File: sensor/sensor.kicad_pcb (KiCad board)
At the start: 2 copper layers, 46.5 x 34 mm, 42 parts, among them J1 5V, J2 CAN IN, J3 CAN OUT, J4 AVR-ISP-6, J5 SENSOR IN, J6 SENSOR VCC, J7 SENSOR GND, U1 ATmega32M1-AU, U2 MCP2551-I-SN, Y1 16MHz

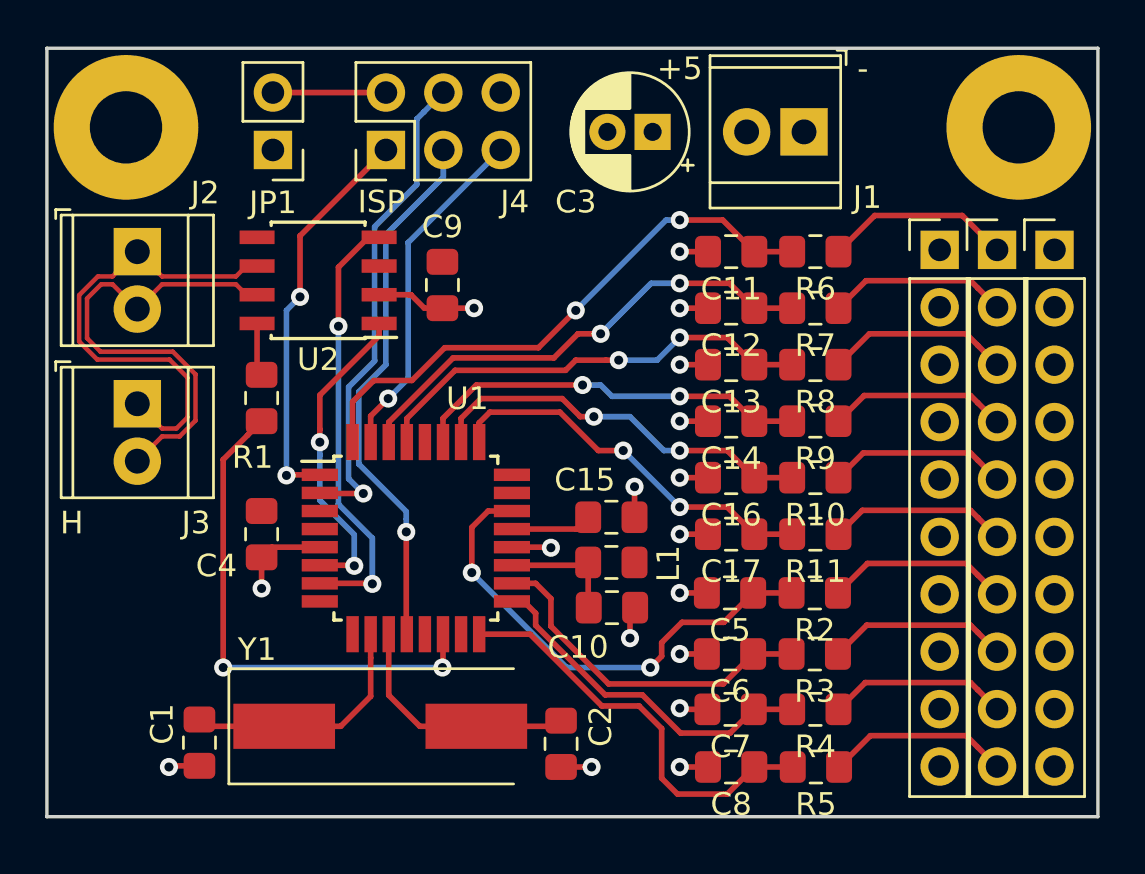
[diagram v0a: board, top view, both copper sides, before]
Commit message: Added power LED to sensor board
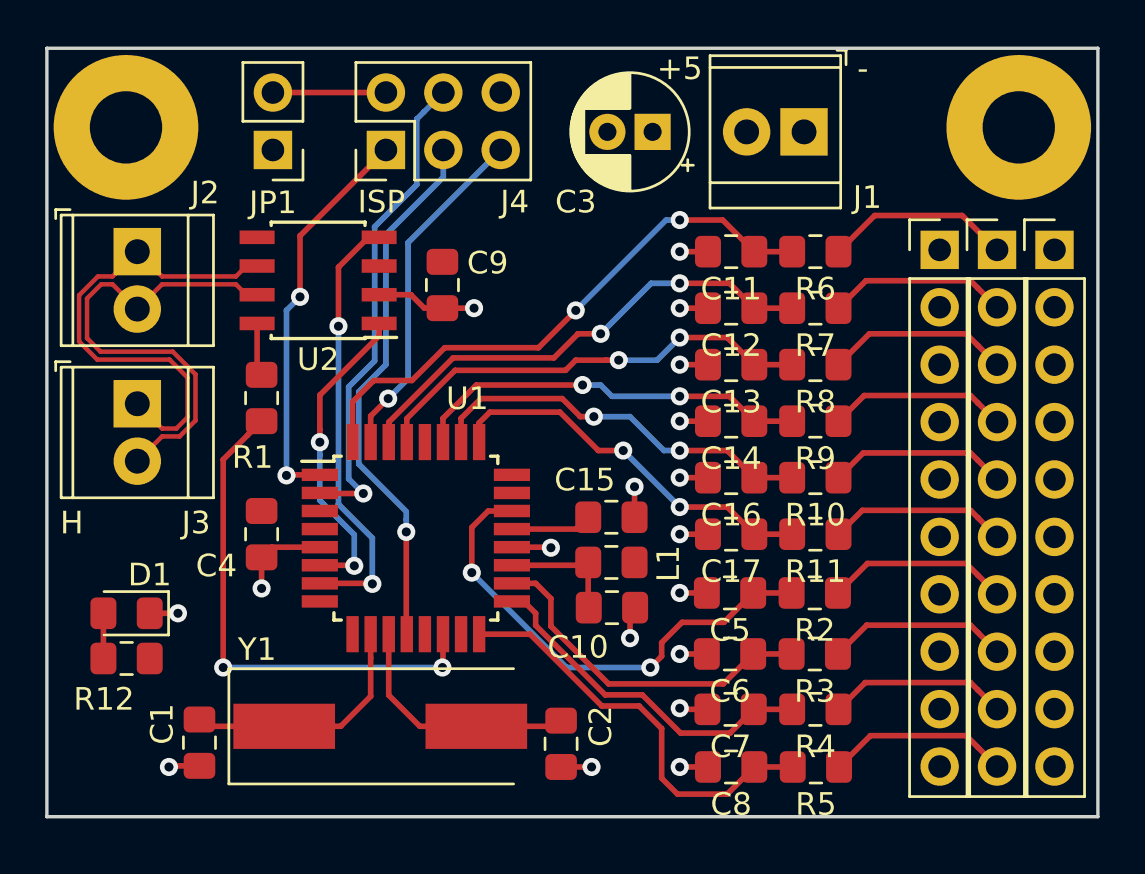
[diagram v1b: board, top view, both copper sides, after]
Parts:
- added D1: POWER, LED_SMD:LED_0805_2012Metric_Pad1.15x1.40mm_HandSolder, F.Cu at (126.5, 87.0)
- added R12: 470, Resistor_SMD:R_0805_2012Metric_Pad1.15x1.40mm_HandSolder, F.Cu at (126.5, 89.0)
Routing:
- net Net-(D1-Pad2): track 0.00 -> 2.00 mm
- net GND: track 28.2 -> 29.5 mm, vias 17 -> 18
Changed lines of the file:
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@@
     (thickness 1.6)
     (drawings 10)
-    (tracks 312)
+    (tracks 315)
     (zones 0)
-    (modules 42)
-    (nets 38)
+    (modules 44)
+    (nets 39)
   )
   (page A4)
@@
   (net 36 /CAN_TXD)
   (net 37 /CAN_RXD)
+  (net 38 "Net-(D1-Pad2)")
   (net_class Default "This is the default net class."
     (clearance 0.2)
@@
     (add_net "Net-(C1-Pad1)")
     (add_net "Net-(C2-Pad2)")
+    (add_net "Net-(D1-Pad2)")
     (add_net "Net-(J4-Pad2)")
     (add_net "Net-(R1-Pad1)")
@@
     (tags "capacitor handsolder")
     (attr smd)
-    (fp_text reference C9 (at -2.575 0) (layer F.SilkS)
+    (fp_text reference C9 (at -0.975 -2) (layer F.SilkS)
       (effects (font (size 1 1) (thickness 0.15)))
     )
@@
     (pad 1 thru_hole circle (at 0 0) (size 6.4 6.4) (drill 3.2) (layers *.Cu *.Mask)
       (net 2 GND))
+  )
+  (module LED_SMD:LED_0805_2012Metric_Pad1.15x1.40mm_HandSolder (layer F.Cu)
+    (at 126.525 87 180)
+    (descr "LED SMD 0805 (2012 Metric), square (rectangular) end terminal, IPC_7351 nominal, (Body size source: https://docs.google.com/spreadsheets/d/1BsfQQcO9C6DZCsRaXUlFlo91Tg2WpOkGARC1WS5S8t0/edit?usp=sharing), generated with kicad-footprint-generator")
+    (tags "LED handsolder")
+    (attr smd)
+    (fp_text reference D1 (at -1.025 1.7 180) (layer F.SilkS)
+      (effects (font (size 1 1) (thickness 0.15)))
+    )
+    (fp_text value POWER (at 0 1.65 180) (layer F.Fab)
+      (effects (font (size 1 1) (thickness 0.15)))
+    )
+    (fp_line (start 1 -0.6) (end -0.7 -0.6) (layer F.Fab) (width 0.1))
+    (fp_line (start -0.7 -0.6) (end -1 -0.3) (layer F.Fab) (width 0.1))
+    (fp_line (start -1 -0.3) (end -1 0.6) (layer F.Fab) (width 0.1))
+    (fp_line (start -1 0.6) (end 1 0.6) (layer F.Fab) (width 0.1))
+    (fp_line (start 1 0.6) (end 1 -0.6) (layer F.Fab) (width 0.1))
+    (fp_line (start 1 -0.96) (end -1.86 -0.96) (layer F.SilkS) (width 0.12))
+    (fp_line (start -1.86 -0.96) (end -1.86 0.96) (layer F.SilkS) (width 0.12))
+    (fp_line (start -1.86 0.96) (end 1 0.96) (layer F.SilkS) (width 0.12))
+    (fp_line (start -1.85 0.95) (end -1.85 -0.95) (layer F.CrtYd) (width 0.05))
+    (fp_line (start -1.85 -0.95) (end 1.85 -0.95) (layer F.CrtYd) (width 0.05))
+    (fp_line (start 1.85 -0.95) (end 1.85 0.95) (layer F.CrtYd) (width 0.05))
+    (fp_line (start 1.85 0.95) (end -1.85 0.95) (layer F.CrtYd) (width 0.05))
+    (fp_text user %R (at 0 0 180) (layer F.Fab)
+      (effects (font (size 0.5 0.5) (thickness 0.08)))
+    )
+    (pad 1 smd roundrect (at -1.025 0 180) (size 1.15 1.4) (layers F.Cu F.Paste F.Mask) (roundrect_rratio 0.217391)
+      (net 2 GND))
+    (pad 2 smd roundrect (at 1.025 0 180) (size 1.15 1.4) (layers F.Cu F.Paste F.Mask) (roundrect_rratio 0.217391)
+      (net 38 "Net-(D1-Pad2)"))
+    (model ${KISYS3DMOD}/LED_SMD.3dshapes/LED_0805_2012Metric.wrl
+      (at (xyz 0 0 0))
+      (scale (xyz 1 1 1))
+      (rotate (xyz 0 0 0))
+    )
+  )
+  (module Resistor_SMD:R_0805_2012Metric_Pad1.15x1.40mm_HandSolder (layer F.Cu)
+    (at 126.525 89)
+    (descr "Resistor SMD 0805 (2012 Metric), square (rectangular) end terminal, IPC_7351 nominal with elongated pad for handsoldering. (Body size source: https://docs.google.com/spreadsheets/d/1BsfQQcO9C6DZCsRaXUlFlo91Tg2WpOkGARC1WS5S8t0/edit?usp=sharing), generated with kicad-footprint-generator")
+    (tags "resistor handsolder")
+    (attr smd)
+    (fp_text reference R12 (at -1 1.8 180) (layer F.SilkS)
+      (effects (font (size 1 1) (thickness 0.15)))
+    )
+    (fp_text value 470 (at 0 1.65) (layer F.Fab)
+      (effects (font (size 1 1) (thickness 0.15)))
+    )
+    (fp_line (start -1 0.6) (end -1 -0.6) (layer F.Fab) (width 0.1))
+    (fp_line (start -1 -0.6) (end 1 -0.6) (layer F.Fab) (width 0.1))
+    (fp_line (start 1 -0.6) (end 1 0.6) (layer F.Fab) (width 0.1))
+    (fp_line (start 1 0.6) (end -1 0.6) (layer F.Fab) (width 0.1))
+    (fp_line (start -0.261252 -0.71) (end 0.261252 -0.71) (layer F.SilkS) (width 0.12))
+    (fp_line (start -0.261252 0.71) (end 0.261252 0.71) (layer F.SilkS) (width 0.12))
+    (fp_line (start -1.85 0.95) (end -1.85 -0.95) (layer F.CrtYd) (width 0.05))
+    (fp_line (start -1.85 -0.95) (end 1.85 -0.95) (layer F.CrtYd) (width 0.05))
+    (fp_line (start 1.85 -0.95) (end 1.85 0.95) (layer F.CrtYd) (width 0.05))
+    (fp_line (start 1.85 0.95) (end -1.85 0.95) (layer F.CrtYd) (width 0.05))
+    (fp_text user %R (at 0 0) (layer F.Fab)
+      (effects (font (size 0.5 0.5) (thickness 0.08)))
+    )
+    (pad 1 smd roundrect (at -1.025 0) (size 1.15 1.4) (layers F.Cu F.Paste F.Mask) (roundrect_rratio 0.217391)
+      (net 38 "Net-(D1-Pad2)"))
+    (pad 2 smd roundrect (at 1.025 0) (size 1.15 1.4) (layers F.Cu F.Paste F.Mask) (roundrect_rratio 0.217391)
+      (net 4 VCC))
+    (model ${KISYS3DMOD}/Resistor_SMD.3dshapes/R_0805_2012Metric.wrl
+      (at (xyz 0 0 0))
+      (scale (xyz 1 1 1))
+      (rotate (xyz 0 0 0))
+    )
   )
   (gr_text H (at 124.1 83) (layer F.SilkS)
@@
   (segment (start 148.8 86.975) (end 149.025 86.75) (width 0.25) (layer F.Cu) (net 2))
   (segment (start 148.8 88.1) (end 148.8 86.975) (width 0.25) (layer F.Cu) (net 2))
+  (via (at 128.8 87) (size 0.8) (drill 0.4) (layers F.Cu B.Cu) (net 2))
+  (segment (start 127.55 87) (end 128.8 87) (width 0.25) (layer F.Cu) (net 2))
   (segment (start 145.5 92) (end 145.75 91.75) (width 0.25) (layer F.Cu) (net 3))
   (segment (start 142 92) (end 145.5 92) (width 0.25) (layer F.Cu) (net 3))
@@
   (segment (start 146.95 86.725) (end 146.975 86.75) (width 0.25) (layer F.Cu) (net 9))
   (segment (start 146.95 84.75) (end 146.95 86.725) (width 0.25) (layer F.Cu) (net 9))
-  (segment (start 155.975 71) (end 154.3 71) (width 0.25) (layer F.Cu) (net 16))
-  (segment (start 155.975 73.5) (end 154.3 73.5) (width 0.25) (layer F.Cu) (net 15))
-  (segment (start 155.975 76) (end 154.3 76) (width 0.25) (layer F.Cu) (net 13))
-  (segment (start 155.975 78.5) (end 154.3 78.5) (width 0.25) (layer F.Cu) (net 12))
-  (segment (start 146.424999 83.275001) (end 146.95 82.75) (width 0.25) (layer F.Cu) (net 14))
-  (segment (start 143.575001 83.275001) (end 146.424999 83.275001) (width 0.25) (layer F.Cu) (net 14))
-  (segment (start 155.975 81) (end 154.3 81) (width 0.25) (layer F.Cu) (net 11))
   (segment (start 155.975 83.5) (end 154.3 83.5) (width 0.25) (layer F.Cu) (net 10))
   (via (at 151 82.3) (size 0.8) (drill 0.4) (layers F.Cu B.Cu) (net 10))
   (segment (start 154.3 83.5) (end 153.1 82.3) (width 0.25) (layer F.Cu) (net 10))
   (segment (start 153.1 82.3) (end 151 82.3) (width 0.25) (layer F.Cu) (net 10))
-  (via (at 151 69.6) (size 0.8) (drill 0.4) (layers F.Cu B.Cu) (net 16))
-  (segment (start 154.3 71) (end 152.9 69.6) (width 0.25) (layer F.Cu) (net 16))
-  (segment (start 152.9 69.6) (end 151 69.6) (width 0.25) (layer F.Cu) (net 16))
   (via (at 148.5 79.8) (size 0.8) (drill 0.4) (layers F.Cu B.Cu) (net 10))
   (segment (start 151 82.3) (end 148.5 79.8) (width 0.25) (layer B.Cu) (net 10))
@@
   (segment (start 142.6 78.1) (end 145.7 78.1) (width 0.25) (layer F.Cu) (net 10))
   (segment (start 148.5 79.8) (end 147.4 79.8) (width 0.25) (layer F.Cu) (net 10))
+  (segment (start 155.975 81) (end 154.3 81) (width 0.25) (layer F.Cu) (net 11))
   (via (at 151 79.8) (size 0.8) (drill 0.4) (layers F.Cu B.Cu) (net 11))
   (segment (start 154.3 81) (end 153.1 79.8) (width 0.25) (layer F.Cu) (net 11))
@@
   (segment (start 148.8 78.3) (end 150.3 79.8) (width 0.25) (layer B.Cu) (net 11))
   (segment (start 147.2 78.3) (end 148.8 78.3) (width 0.25) (layer B.Cu) (net 11))
+  (segment (start 155.975 78.5) (end 154.3 78.5) (width 0.25) (layer F.Cu) (net 12))
   (via (at 151 77.4) (size 0.8) (drill 0.4) (layers F.Cu B.Cu) (net 12))
   (segment (start 154.3 78.5) (end 153.2 77.4) (width 0.25) (layer F.Cu) (net 12))
@@
   (segment (start 148 77.4) (end 151 77.4) (width 0.25) (layer B.Cu) (net 12))
   (segment (start 146.7 76.9) (end 147.5 76.9) (width 0.25) (layer B.Cu) (net 12))
+  (segment (start 155.975 76) (end 154.3 76) (width 0.25) (layer F.Cu) (net 13))
   (via (at 151 74.8) (size 0.8) (drill 0.4) (layers F.Cu B.Cu) (net 13))
   (segment (start 150 75.8) (end 148.3 75.8) (width 0.25) (layer B.Cu) (net 13))
@@
   (segment (start 138.925001 78.384411) (end 141.059401 76.250011) (width 0.25) (layer F.Cu) (net 13))
   (segment (start 146.4 75.8) (end 147.734315 75.8) (width 0.25) (layer F.Cu) (net 13))
+  (segment (start 146.424999 83.275001) (end 146.95 82.75) (width 0.25) (layer F.Cu) (net 14))
+  (segment (start 143.575001 83.275001) (end 146.424999 83.275001) (width 0.25) (layer F.Cu) (net 14))
+  (segment (start 155.975 73.5) (end 154.3 73.5) (width 0.25) (layer F.Cu) (net 15))
   (via (at 151 72.4) (size 0.8) (drill 0.4) (layers F.Cu B.Cu) (net 15))
   (segment (start 154.3 73.5) (end 153.2 72.4) (width 0.25) (layer F.Cu) (net 15))
@@
   (segment (start 147.5 74.634315) (end 149.734315 72.4) (width 0.25) (layer B.Cu) (net 15))
   (segment (start 149.734315 72.4) (end 151 72.4) (width 0.25) (layer B.Cu) (net 15))
+  (segment (start 155.975 71) (end 154.3 71) (width 0.25) (layer F.Cu) (net 16))
+  (via (at 151 69.6) (size 0.8) (drill 0.4) (layers F.Cu B.Cu) (net 16))
+  (segment (start 154.3 71) (end 152.9 69.6) (width 0.25) (layer F.Cu) (net 16))
+  (segment (start 152.9 69.6) (end 151 69.6) (width 0.25) (layer F.Cu) (net 16))
   (via (at 146.4 73.6) (size 0.8) (drill 0.4) (layers F.Cu B.Cu) (net 16))
   (segment (start 150.4 69.6) (end 151 69.6) (width 0.25) (layer B.Cu) (net 16))
@@
   (segment (start 135.9 74.3) (end 135.9 82.172958) (width 0.25) (layer B.Cu) (net 37))
   (segment (start 135.9 82.172958) (end 135.899978 82.17298) (width 0.25) (layer B.Cu) (net 37))
+  (segment (start 125.5 89) (end 125.5 87) (width 0.25) (layer F.Cu) (net 38))
   (zone (net 4) (net_name VCC) (layer F.Cu) (hatch edge 0.508)
     (connect_pads (clearance 0.2))

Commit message: sensor: modernize
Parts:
- removed J3: CAN OUT, TerminalBlock_TE-Connectivity:TerminalBlock_TE_282834-2_1x02_P2.54mm_Horizontal
- added C18: 100n, Capacitor_SMD:C_0805_2012Metric_Pad1.15x1.40mm_HandSolder, F.Cu at (154.8, 67.2)
- added H3: SW, MountingHole:MountingHole_3.2mm_M3_Pad, F.Cu at (126.5, 92.5)
- added R13: DNP/0, Resistor_SMD:R_0805_2012Metric_Pad1.15x1.40mm_HandSolder, F.Cu at (147.9, 70.9)
- added U3: LM2937xMP, Package_TO_SOT_SMD:SOT-223-3_TabPin2, F.Cu at (149.3, 66.0)
- C3: footprint Capacitor_THT:CP_Radial_D5.0mm_P2.00mm -> Capacitor_SMD:C_0805_2012Metric_Pad1.15x1.40mm_HandSolder
- J1: value 5V -> 12V
- J2: value CAN IN -> CAN; footprint TerminalBlock_TE-Connectivity:TerminalBlock_TE_282834-2_1x02_P2.54mm_Horizontal -> TerminalBlock_TE-Connectivity:TerminalBlock_TE_282834-6_1x06_P2.54mm_Horizontal
- moved C3 7.89 mm to (144.8, 71.8), turned to 270 degrees
- moved C1 5.90 mm to (132.5, 87.5), turned to 90 degrees
- moved J1 3.91 mm to (160.4, 65.9)
- moved R12 3.43 mm to (129.7, 87.7), turned to 90 degrees
- moved C2 1.17 mm to (146.6, 93.6), turned to 180 degrees
- moved D1 0.93 mm to (126.3, 87.9), turned to 0 degrees
- moved J2 0.20 mm to (126.8, 71.0)
- moved J4 0.10 mm to (137.9, 66.5)
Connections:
- J1 pad 2: VCC -> Net-(C18-Pad1)
- J2 pad 1: /CAN_N -> GND
- J2 pad 2: /CAN_P -> /CAN_N
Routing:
- net GND: track 29.5 -> 41.4 mm, vias 18 -> 24
- net Net-(C18-Pad1): track 0.00 -> 11.5 mm
- net /CAN_P: track 21.5 -> 15.9 mm
- net /CAN_N: track 21.5 -> 17.1 mm
- net /CAN_HISPEED: track 22.8 -> 19.5 mm
- added copper zone on F.Cu, net GND
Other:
- board text added: "+"
- board text removed: "+5"
- board text removed: "H"
